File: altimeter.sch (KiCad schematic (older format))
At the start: 42 parts, among them Q101 DMG2301L, Q102 NTR4003NT1G, Q103 SISS05dn, U1 LMV331, U101 STM32F303CCTx, U102 S25FL512SAGMFIR11, U103 AIS2120SXTR, U104 MIC5219-3.3YM5, U105 LF50_TO252, U106 BMI088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

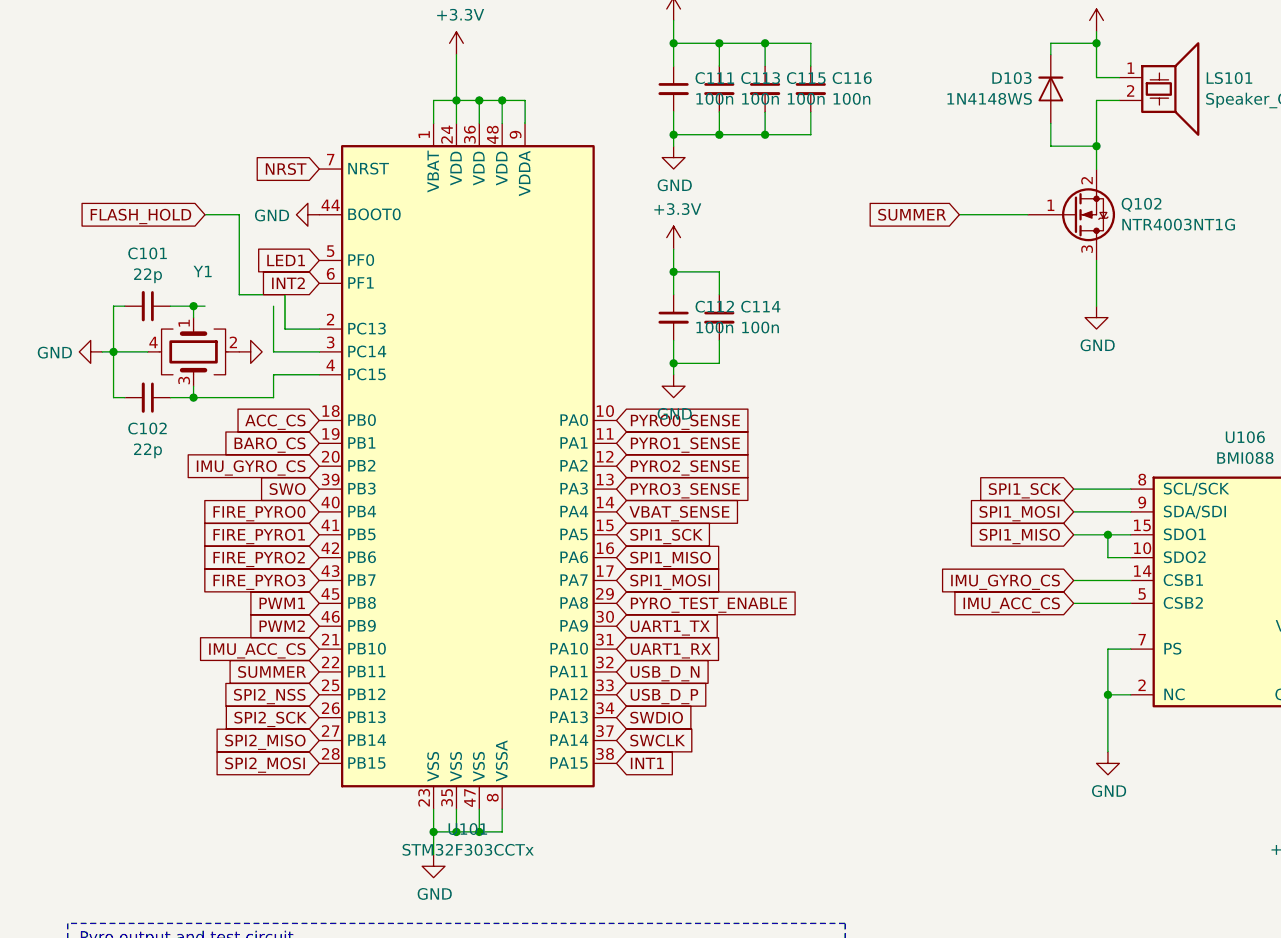
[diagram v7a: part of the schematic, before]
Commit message: fix wrong connection of quarz
Signed-off-by: Thomas Schmid <tom@binary-kitchen.de>
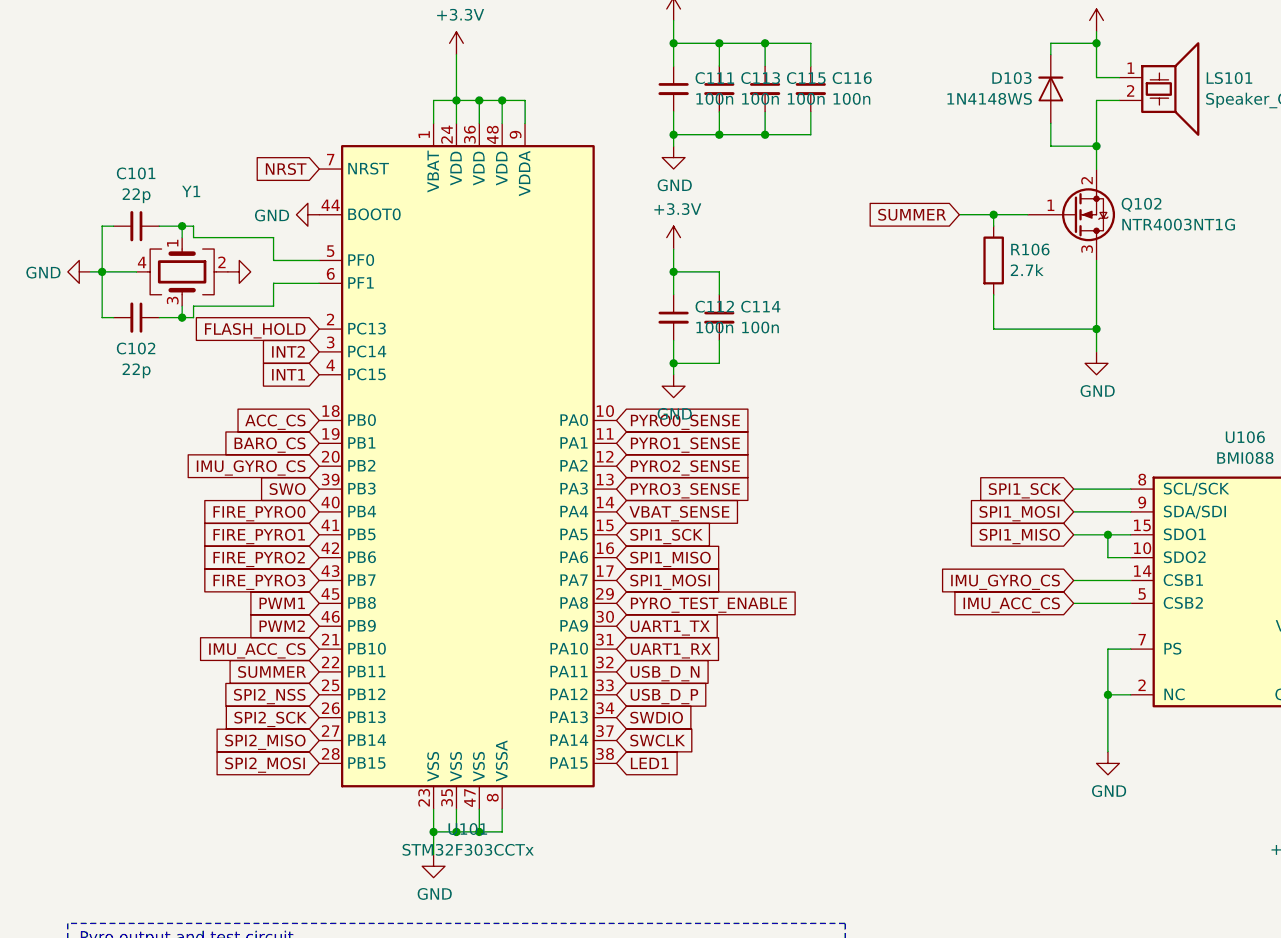
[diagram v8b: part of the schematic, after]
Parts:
- added R106: 2.7k, Resistor_SMD:R_0402_1005Metric, symbol Device:R
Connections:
- net GND: now also R106.2
- net INT1: now also U101.4 (PC15); no longer U101.38 (PA15)
- net INT2: now also U101.3 (PC14); no longer U101.6 (PF1)
- net LED1: now also U101.38 (PA15); no longer U101.5 (PF0)
- net SUMMER: now also R106.1
- net at C101.1, Y1.1: now also U101.5 (PF0)
- net at C102.1, Y1.3: now also U101.6 (PF1); no longer U101.4 (PC15)
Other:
- moved on the sheet: C101, C102, Y1
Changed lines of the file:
@@
 	2550 4200 2550 4100
 Connection ~ 2450 4200
-Wire Wire Line
-	1550 2200 1750 2200
-Wire Wire Line
-	1550 2100 1750 2100
 $Comp
 L Device:C_Small C101
 U 1 1 5D4147AB
-P 1000 1900
-F 0 "C101" V 771 1900 50  0000 C CNN
-F 1 "22p" V 862 1900 50  0000 C CNN
-F 2 "Capacitor_SMD:C_0402_1005Metric" H 1000 1900 50  0001 C CNN
-F 3 "~" H 1000 1900 50  0001 C CNN
-F 4 "https://www.mouser.de/ProductDetail/Murata-Electronics/GCM1555G1H220JA16D?qs=sGAEpiMZZMs0AnBnWHyRQAsAWwhBCY7bDLShlSp46t28ceXO6IsPuQ%3D%3D" H 1000 1900 50  0001 C CNN "Mouser_Link"
-F 5 "GCM1555G1H220JA16D" H 1000 1900 50  0001 C CNN "Parnumber"
-	1    1000 1900
+P 950 1550
+F 0 "C101" V 721 1550 50  0000 C CNN
+F 1 "22p" V 812 1550 50  0000 C CNN
+F 2 "Capacitor_SMD:C_0402_1005Metric" H 950 1550 50  0001 C CNN
+F 3 "~" H 950 1550 50  0001 C CNN
+F 4 "https://www.mouser.de/ProductDetail/Murata-Electronics/GCM1555G1H220JA16D?qs=sGAEpiMZZMs0AnBnWHyRQAsAWwhBCY7bDLShlSp46t28ceXO6IsPuQ%3D%3D" H 950 1550 50  0001 C CNN "Mouser_Link"
+F 5 "GCM1555G1H220JA16D" H 950 1550 50  0001 C CNN "Parnumber"
+	1    950  1550
 	0    1    1    0
 $EndComp
@@
 L Device:C_Small C102
 U 1 1 5D415036
-P 1000 2300
-F 0 "C102" V 1137 2300 50  0000 C CNN
-F 1 "22p" V 1228 2300 50  0000 C CNN
-F 2 "Capacitor_SMD:C_0402_1005Metric" H 1000 2300 50  0001 C CNN
-F 3 "~" H 1000 2300 50  0001 C CNN
-F 4 "https://www.mouser.de/ProductDetail/Murata-Electronics/GCM1555G1H220JA16D?qs=sGAEpiMZZMs0AnBnWHyRQAsAWwhBCY7bDLShlSp46t28ceXO6IsPuQ%3D%3D" H 1000 2300 50  0001 C CNN "Mouser_Link"
-F 5 "GCM1555G1H220JA16D" H 1000 2300 50  0001 C CNN "Parnumber"
-	1    1000 2300
+P 950 1950
+F 0 "C102" V 1087 1950 50  0000 C CNN
+F 1 "22p" V 1178 1950 50  0000 C CNN
+F 2 "Capacitor_SMD:C_0402_1005Metric" H 950 1950 50  0001 C CNN
+F 3 "~" H 950 1950 50  0001 C CNN
+F 4 "https://www.mouser.de/ProductDetail/Murata-Electronics/GCM1555G1H220JA16D?qs=sGAEpiMZZMs0AnBnWHyRQAsAWwhBCY7bDLShlSp46t28ceXO6IsPuQ%3D%3D" H 950 1950 50  0001 C CNN "Mouser_Link"
+F 5 "GCM1555G1H220JA16D" H 950 1950 50  0001 C CNN "Parnumber"
+	1    950  1950
 	0    1    1    0
 $EndComp
@@
 L power:GND #PWR0101
 U 1 1 5D4163E2
-P 800 2100
-F 0 "#PWR0101" H 800 1850 50  0001 C CNN
-F 1 "GND" V 805 1972 50  0000 R CNN
-F 2 "" H 800 2100 50  0001 C CNN
-F 3 "" H 800 2100 50  0001 C CNN
-	1    800  2100
+P 750 1750
+F 0 "#PWR0101" H 750 1500 50  0001 C CNN
+F 1 "GND" V 755 1622 50  0000 R CNN
+F 2 "" H 750 1750 50  0001 C CNN
+F 3 "" H 750 1750 50  0001 C CNN
+	1    750  1750
 	0    1    1    0
 $EndComp
@@
 	0    -1   -1   0
 $EndComp
-Text GLabel 1750 1700 0    50   Input ~ 0
+Text GLabel 3050 3900 2    50   Input ~ 0
 LED1
 $Comp
@@
 L Device:Crystal_GND24 Y1
 U 1 1 5D515671
-P 1200 2100
-F 0 "Y1" V 850 2100 50  0000 L CNN
-F 1 "Crystal_GND24" V 950 2100 50  0001 L CNN
-F 2 "Crystal:Crystal_SMD_2520-4Pin_2.5x2.0mm" H 1200 2100 50  0001 C CNN
-F 3 "http://www5.epsondevice.com/en/products/crystal_unit/tsx3225.html#" H 1200 2100 50  0001 C CNN
-F 4 "https://www.mouser.de/ProductDetail/Epson-Timing/TSX-3225-240000MF15X-AC3?qs=sGAEpiMZZMsBj6bBr9Q9acukpafrIaZ11siWonQt25M%3D" V 1200 2100 50  0001 C CNN "Mouser_Link"
-F 5 "TSX-3225 24.0000MF15X-AC3 " V 1200 2100 50  0001 C CNN "Parnumber"
-	1    1200 2100
+P 1150 1750
+F 0 "Y1" V 800 1750 50  0000 L CNN
+F 1 "Crystal_GND24" V 900 1750 50  0001 L CNN
+F 2 "Crystal:Crystal_SMD_2520-4Pin_2.5x2.0mm" H 1150 1750 50  0001 C CNN
+F 3 "http://www5.epsondevice.com/en/products/crystal_unit/tsx3225.html#" H 1150 1750 50  0001 C CNN
+F 4 "https://www.mouser.de/ProductDetail/Epson-Timing/TSX-3225-240000MF15X-AC3?qs=sGAEpiMZZMsBj6bBr9Q9acukpafrIaZ11siWonQt25M%3D" V 1150 1750 50  0001 C CNN "Mouser_Link"
+F 5 "TSX-3225 24.0000MF15X-AC3 " V 1150 1750 50  0001 C CNN "Parnumber"
+	1    1150 1750
 	0    1    1    0
 $EndComp
 Wire Wire Line
-	1200 1950 1200 1900
-Wire Wire Line
-	1200 2250 1200 2300
-Wire Wire Line
-	1100 2300 1200 2300
-Connection ~ 1200 2300
-Wire Wire Line
-	800  2100 850  2100
-Wire Wire Line
-	900  2300 850  2300
-Wire Wire Line
-	850  2300 850  2100
-Connection ~ 850  2100
-Wire Wire Line
-	850  2100 1000 2100
-Connection ~ 1200 1900
-Wire Wire Line
-	900  1900 850  1900
-Wire Wire Line
-	850  1900 850  2100
+	1150 1600 1150 1550
+Wire Wire Line
+	1150 1900 1150 1950
+Wire Wire Line
+	750  1750 800  1750
+Wire Wire Line
+	800  1950 800  1750
+Connection ~ 800  1750
+Wire Wire Line
+	800  1750 950  1750
+Wire Wire Line
+	850  1550 800  1550
+Wire Wire Line
+	800  1550 800  1750
 $Comp
 L power:GND #PWR0131
 U 1 1 5D547996
-P 1400 2100
-F 0 "#PWR0131" H 1400 1850 50  0001 C CNN
-F 1 "GND" V 1405 1972 50  0001 R CNN
-F 2 "" H 1400 2100 50  0001 C CNN
-F 3 "" H 1400 2100 50  0001 C CNN
-	1    1400 2100
+P 1350 1750
+F 0 "#PWR0131" H 1350 1500 50  0001 C CNN
+F 1 "GND" V 1355 1622 50  0001 R CNN
+F 2 "" H 1350 1750 50  0001 C CNN
+F 3 "" H 1350 1750 50  0001 C CNN
+	1    1350 1750
 	0    -1   -1   0
 $EndComp
@@
 L power:GND #PWR0139
 U 1 1 5D56CD7F
-P 5150 1900
-F 0 "#PWR0139" H 5150 1650 50  0001 C CNN
-F 1 "GND" H 5155 1727 50  0000 C CNN
-F 2 "" H 5150 1900 50  0001 C CNN
-F 3 "" H 5150 1900 50  0001 C CNN
-	1    5150 1900
-	1    0    0    -1
-$EndComp
-Wire Wire Line
-	5150 1900 5150 1700
+P 5150 2100
+F 0 "#PWR0139" H 5150 1850 50  0001 C CNN
+F 1 "GND" H 5155 1927 50  0000 C CNN
+F 2 "" H 5150 2100 50  0001 C CNN
+F 3 "" H 5150 2100 50  0001 C CNN
+	1    5150 2100
+	1    0    0    -1
+$EndComp
+Wire Wire Line
+	5150 2100 5150 2000
 $Comp
 L power:+5V #PWR0140
@@
 SUMMER
 Wire Wire Line
-	4550 1500 4850 1500
+	4550 1500 4700 1500
 Wire Wire Line
 	4950 800  4950 750
@@
 Text GLabel 1750 2600 0    50   Input ~ 0
 IMU_GYRO_CS
-Wire Wire Line
-	1550 1900 1550 2100
-Wire Wire Line
-	1200 1900 1250 1900
-Wire Wire Line
-	1550 2200 1550 2300
-Wire Wire Line
-	1200 2300 1550 2300
 $Comp
 L power:+3.3V #PWR0143
@@
 Text GLabel 6300 2900 2    50   Input ~ 0
 INT2
-Text GLabel 3050 3900 2    50   Input ~ 0
+Text GLabel 1750 2200 0    50   Input ~ 0
 INT1
-Text GLabel 1750 1800 0    50   Input ~ 0
+Text GLabel 1750 2100 0    50   Input ~ 0
 INT2
 $Comp
@@
 Text GLabel 5300 5500 0    50   Input ~ 0
 FLASH_HOLD
-Text GLabel 1250 1500 0    50   Input ~ 0
+Text GLabel 1750 2000 0    50   Input ~ 0
 FLASH_HOLD
-Wire Wire Line
-	1750 2000 1600 2000
-Wire Wire Line
-	1600 2000 1600 1850
-Wire Wire Line
-	1600 1850 1400 1850
-Wire Wire Line
-	1400 1850 1400 1500
-Wire Wire Line
-	1400 1500 1250 1500
 $Comp
 L power:+BATT #PWR0162
@@
 $EndComp
 Wire Wire Line
-	1100 1900 1200 1900
+	1050 1550 1150 1550
+Wire Wire Line
+	1050 1950 1150 1950
+Wire Wire Line
+	850  1950 800  1950
+Wire Wire Line
+	1150 1950 1200 1950
+Wire Wire Line
+	1200 1950 1200 1900
+Wire Wire Line
+	1200 1900 1550 1900
+Wire Wire Line
+	1550 1900 1550 1800
+Wire Wire Line
+	1550 1800 1750 1800
+Connection ~ 1150 1950
+Wire Wire Line
+	1750 1700 1550 1700
+Wire Wire Line
+	1550 1700 1550 1600
+Wire Wire Line
+	1550 1600 1200 1600
+Wire Wire Line
+	1200 1600 1200 1550
+Wire Wire Line
+	1200 1550 1150 1550
+Connection ~ 1150 1550
+$Comp
+L Device:R R106
+U 1 1 5D87B7D0
+P 4700 1700
+F 0 "R106" H 4770 1746 50  0000 L CNN
+F 1 "2.7k" H 4770 1655 50  0000 L CNN
+F 2 "Resistor_SMD:R_0402_1005Metric" V 4630 1700 50  0001 C CNN
+F 3 "~" H 4700 1700 50  0001 C CNN
+	1    4700 1700
+	1    0    0    -1
+$EndComp
+Wire Wire Line
+	4700 1550 4700 1500
+Connection ~ 4700 1500
+Wire Wire Line
+	4700 1500 4850 1500
+Wire Wire Line
+	4700 1850 4700 2000
+Wire Wire Line
+	4700 2000 5150 2000
+Connection ~ 5150 2000
+Wire Wire Line
+	5150 2000 5150 1700
 $EndSCHEMATC
